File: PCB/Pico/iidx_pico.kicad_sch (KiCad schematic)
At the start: 77 parts, among them J1 Spin, J2 Spin, J3 RGB, J4 RGB, J5 Spin, J6 Spin, SW1 SWITCH_SPST, SW10 SWITCH_SPST, SW11 SWITCH_SPST, SW12 Tact_4pin, SW13 Tact_4pin, SW2 SWITCH_SPST, SW3 SWITCH_SPST, SW4 SWITCH_SPST, SW5 SWITCH_SPST, SW6 SWITCH_SPST, SW7 SWITCH_SPST, SW8 SWITCH_SPST, SW9 SWITCH_SPST, U1 PiPico_No_SWD, U2 TMAG5273, U3 AS5600

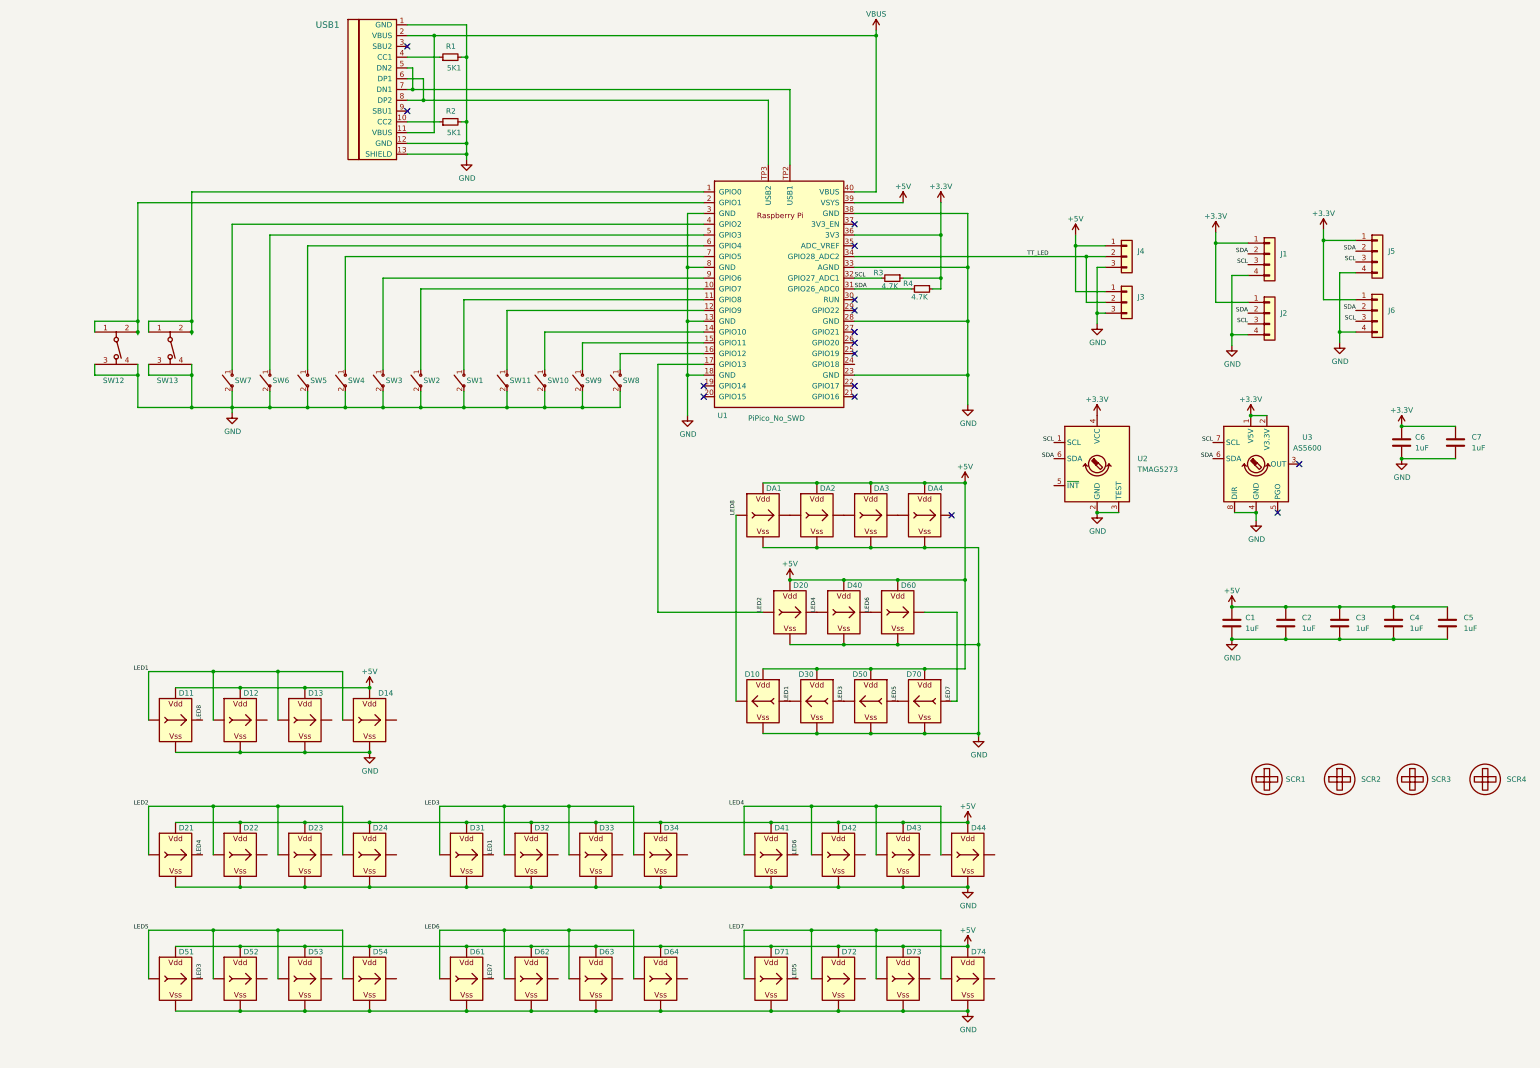
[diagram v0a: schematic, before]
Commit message: Hall effect switch support
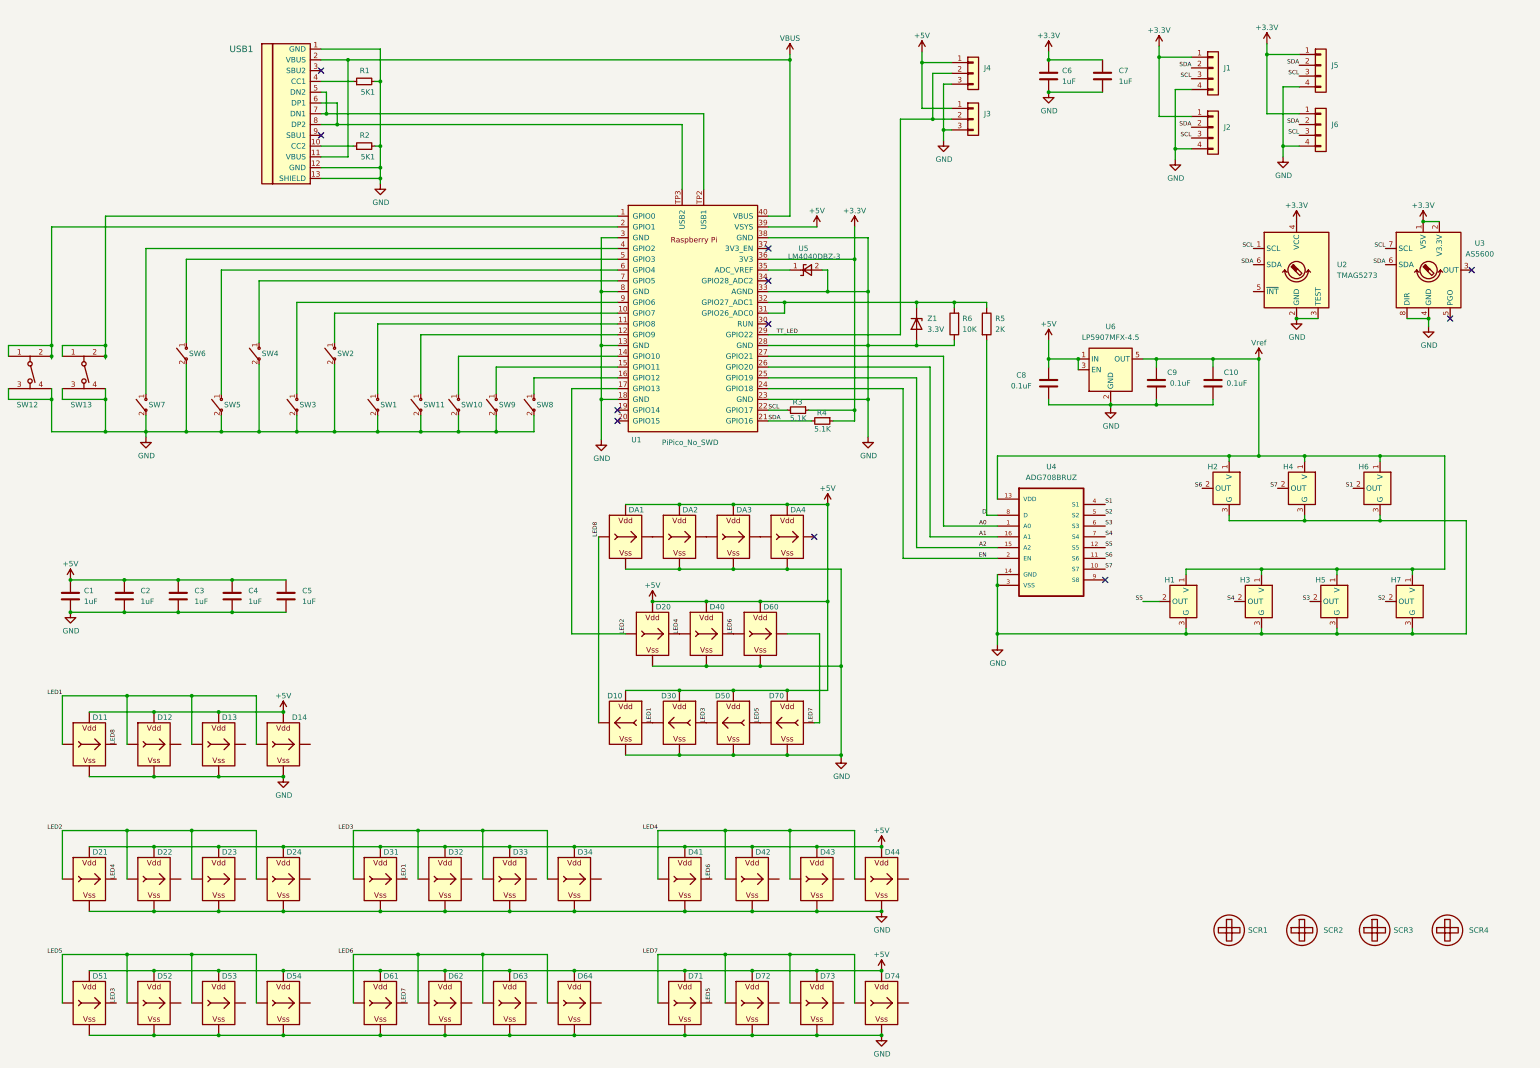
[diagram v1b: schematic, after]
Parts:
- added C10, C8, C9: 0.1uF, Capacitor_SMD:C_0603_1608Metric_Pad1.08x0.95mm_HandSolder, symbol Device:C
- added H1, H2, H3, H4, H5, H6, H7: SS49E_SOT23, iidx_pico:SOT-23-FAT, symbol iidx_pico:SS49E_SOT23
- added R5: 2K, Resistor_SMD:R_0603_1608Metric_Pad0.98x0.95mm_HandSolder, symbol Device:R
- added R6: 10K, Resistor_SMD:R_0603_1608Metric_Pad0.98x0.95mm_HandSolder, symbol Device:R
- added U4: ADG708BRUZ, Package_SO:TSSOP-16_4.4x5mm_P0.65mm, symbol voltex_pico:ADG708BRUZ
- added U5: LM4040DBZ-3, iidx_pico:SOT-23-FAT, symbol Reference_Voltage:LM4040DBZ-3
- added U6: LP5907MFX-4.5, Package_TO_SOT_SMD:SOT-23-5, symbol Regulator_Linear:LP5907MFX-4.5
- added Z1: 3.3V, Diode_SMD:D_SOD-123F, symbol Device:D_Zener
- R3, R4: value 4.7K -> 5.1K
- SW1, SW2, SW3, SW4, SW5, SW6, SW7: footprint iidx_pico:SW_Kailh_Choc_V1V2_IIDX -> iidx_pico:SW_Kailh_Choc_HE_IIDX
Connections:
- net +5V: now also C8.1, U6.1 (IN), U6.3 (EN)
- net GND: now also C10.2, C8.2, C9.2, H1.3 (G), H2.3 (G), H3.3 (G), H4.3 (G), H5.3 (G), H6.3 (G), H7.3 (G), R6.1, U4.14 (GND), U4.3 (VSS), U5.2 (A), U6.2 (GND), Z1.2 (A)
- net SCL: now also U1.22 (GPIO17); no longer U1.32 (GPIO27_ADC1)
- net SDA: now also U1.21 (GPIO16); no longer U1.31 (GPIO26_ADC0)
- net TT_LED: now also U1.29 (GPIO22); no longer U1.34 (GPIO28_ADC2)
- net EN: now reaches U1.24 (GPIO18)
- net EN: now also U4.2 (EN)
- net A2: now reaches U1.25 (GPIO19)
- net A2: now also U4.15 (A2)
- net A1: now reaches U1.26 (GPIO20)
- net A1: now also U4.16 (A1)
- net A0: now reaches U1.27 (GPIO21)
- net A0: now also U4.1 (A0)
- net at U1.35 (ADC_VREF): now also U5.1 (K)
- new net: R5.1, R6.2, U1.31 (GPIO26_ADC0), U1.32 (GPIO27_ADC1), Z1.1 (K)
- new net D: R5.2, U4.8 (D)
- new net S1: H6.2 (OUT), U4.4 (S1)
- new net S2: H7.2 (OUT), U4.5 (S2)
- new net S3: H5.2 (OUT), U4.6 (S3)
- new net S4: H3.2 (OUT), U4.7 (S4)
- new net S5: H1.2 (OUT), U4.12 (S5)
- new net S6: H2.2 (OUT), U4.11 (S6)
- new net S7: H4.2 (OUT), U4.10 (S7)
- new net Vref: C10.1, C9.1, H1.1 (V), H2.1 (V), H3.1 (V), H4.1 (V), H5.1 (V), H6.1 (V), H7.1 (V), U4.13 (VDD), U6.5 (OUT)
- no-connect marks 16 -> 11
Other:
- moved on the sheet: C1, C2, C3, C4, C5, C6, C7, D10, D11, D12, D13, D14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

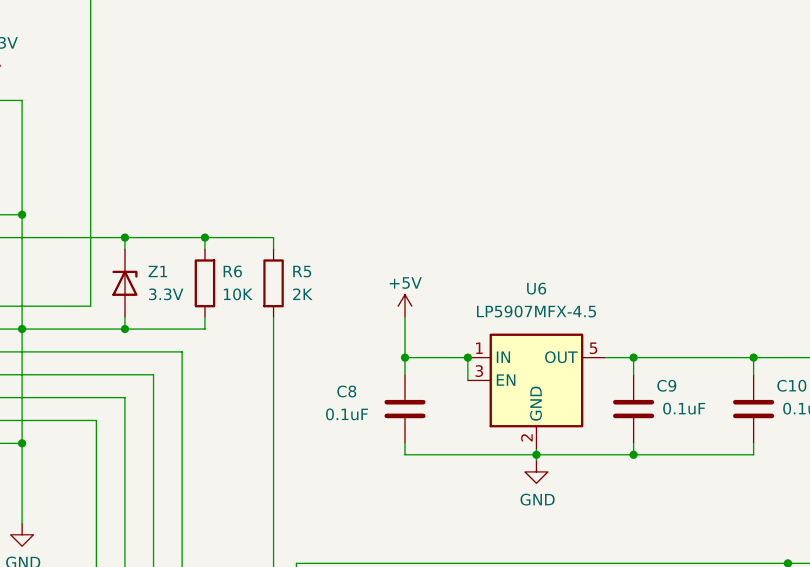
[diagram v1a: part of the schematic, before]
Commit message: PCB Pico v1.53 (vref from vbus)
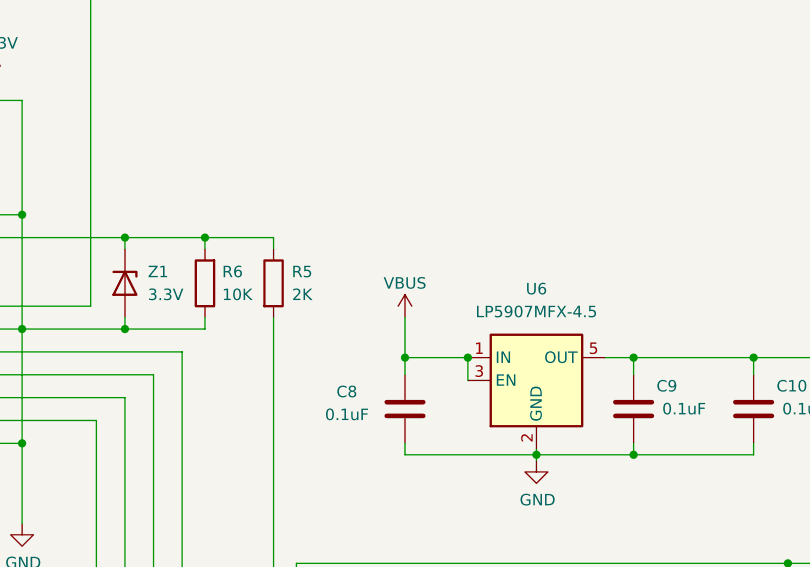
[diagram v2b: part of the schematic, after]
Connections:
- net +5V: no longer C8.1, U6.1 (IN), U6.3 (EN)
- net VBUS: now also C8.1, U6.1 (IN), U6.3 (EN)
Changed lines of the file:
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@@
-	)
-	(symbol
-		(lib_id "power:+5V")
-		(at 277.495 100.965 0)
-		(unit 1)
-		(exclude_from_sim no)
-		(in_bom yes)
-		(on_board yes)
-		(dnp no)
-		(property "Reference" "#PWR016"
-			(at 277.495 104.775 0)
-			(effects
-				(font
-					(size 1.27 1.27)
-				)
-				(hide yes)
-			)
-		)
-		(property "Value" "+5V"
-			(at 277.495 97.155 0)
-			(effects
-				(font
-					(size 1.27 1.27)
-				)
-			)
-		)
-		(property "Footprint" ""
-			(at 277.495 100.965 0)
-			(effects
-				(font
-					(size 1.27 1.27)
-				)
-				(hide yes)
-			)
-		)
-		(property "Datasheet" ""
-			(at 277.495 100.965 0)
-			(effects
-				(font
-					(size 1.27 1.27)
-				)
-				(hide yes)
-			)
-		)
-		(property "Description" ""
-			(at 277.495 100.965 0)
-			(effects
-				(font
-					(size 1.27 1.27)
-				)
-				(hide yes)
-			)
-		)
-		(pin "1"
-		)
-		(instances
-			(project "iidx_pico"
-				(path "/2e3f5573-c264-4a8b-a2f0-0e6473d39aad"
-					(reference "#PWR016")
-					(unit 1)
-				)
-			)
-		)
 	)
 	(symbol
@@
 					(unit 1)
 				)
+			)
+		)
+	)
+	(symbol
+		(lib_id "power:+5V")
+		(at 277.495 100.965 0)
+		(unit 1)
+		(exclude_from_sim no)
+		(in_bom yes)
+		(on_board yes)
+		(dnp no)
+		(property "Reference" "#PWR016"
+			(at 277.495 104.775 0)
+			(effects
+				(font
+					(size 1.27 1.27)
+				)
+				(hide yes)
+			)
+		)
+		(property "Value" "VBUS"
+			(at 277.495 97.155 0)
+			(effects
+				(font
+					(size 1.27 1.27)
+				)
+			)
+		)
+		(property "Footprint" ""
+			(at 277.495 100.965 0)
+			(effects
+				(font
+					(size 1.27 1.27)
+				)
+				(hide yes)
+			)
+		)
+		(property "Datasheet" ""
+			(at 277.495 100.965 0)
+			(effects
+				(font
+					(size 1.27 1.27)
+				)
+				(hide yes)
+			)
+		)
+		(property "Description" ""
+			(at 277.495 100.965 0)
+			(effects
+				(font
+					(size 1.27 1.27)
+				)
+				(hide yes)
+			)
+		)
+		(pin "1"
+		)
+		(instances
+			(project "iidx_pico"
+				(path "/2e3f5573-c264-4a8b-a2f0-0e6473d39aad"
+					(reference "#PWR016")
+					(unit 1)
+				)

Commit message: Update PCB v1.6 files missed
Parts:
- added JP1: DIR, Jumper:SolderJumper-2_P1.3mm_Open_RoundedPad1.0x1.5mm, symbol Jumper:SolderJumper_2_Open
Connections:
- net GND: now also JP1.2 (B); no longer U3.8 (DIR)
- new net: JP1.1 (A), U3.8 (DIR)
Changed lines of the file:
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@@
 	)
 	(junction
+		(at 369.57 99.695)
+		(diameter 0)
+		(color 0 0 0 0)
+	)
+	(junction
 		(at 203.2 183.515)
 		(diameter 0)
@@
 	)
 	(junction
-		(at 367.03 95.885)
-		(diameter 0)
-		(color 0 0 0 0)
-	)
-	(junction
 		(at 309.88 170.18)
 		(diameter 0)
@@
 	(wire
 		(pts
+			(xy 369.57 99.695) (xy 369.57 101.6)
+		)
+		(stroke
+			(width 0)
+			(type default)
+		)
+	)
+	(wire
+		(pts
 			(xy 332.74 57.785) (xy 332.74 55.245)
 		)
@@
 	(wire
 		(pts
-			(xy 367.03 97.79) (xy 367.03 95.885)
-		)
-		(stroke
-			(width 0)
-			(type default)
-		)
-	)
-	(wire
-		(pts
 			(xy 207.645 264.795) (xy 222.885 264.795)
 		)
@@
 	(wire
 		(pts
+			(xy 361.95 95.885) (xy 361.95 99.695)
+		)
+		(stroke
+			(width 0)
+			(type default)
+		)
+	)
+	(wire
+		(pts
 			(xy 42.545 104.775) (xy 42.545 105.41)
 		)
@@
 	(wire
 		(pts
+			(xy 369.57 95.885) (xy 367.03 95.885)
+		)
+		(stroke
+			(width 0)
+			(type default)
+		)
+	)
+	(wire
+		(pts
 			(xy 207.645 249.555) (xy 222.885 249.555)
 		)
@@
 	(wire
 		(pts
-			(xy 361.95 95.885) (xy 367.03 95.885)
-		)
-		(stroke
-			(width 0)
-			(type default)
-		)
-	)
-	(wire
-		(pts
 			(xy 277.495 107.315) (xy 277.495 105.41)
 		)
@@
 	(wire
 		(pts
+			(xy 369.57 95.885) (xy 369.57 99.695)
+		)
+		(stroke
+			(width 0)
+			(type default)
+		)
+	)
+	(wire
+		(pts
 			(xy 129.54 99.695) (xy 129.54 113.665)
 		)
@@
 	(symbol
 		(lib_id "power:GND")
-		(at 367.03 97.79 0)
+		(at 369.57 101.6 0)
 		(unit 1)
 		(exclude_from_sim no)
@@
 		(dnp no)
 		(property "Reference" "#PWR014"
-			(at 367.03 104.14 0)
+			(at 369.57 107.95 0)
 			(effects
 				(font
@@
 		)
 		(property "Value" "GND"
-			(at 367.157 102.1842 0)
+			(at 369.697 105.9942 0)
 			(effects
 				(font
@@
 		)
 		(property "Footprint" ""
-			(at 367.03 97.79 0)
+			(at 369.57 101.6 0)
 			(effects
 				(font
@@
 		)
 		(property "Datasheet" ""
-			(at 367.03 97.79 0)
+			(at 369.57 101.6 0)
 			(effects
 				(font
@@
 		)
 		(property "Description" ""
-			(at 367.03 97.79 0)
+			(at 369.57 101.6 0)
 			(effects
 				(font
@@
 					(unit 1)
 				)
+			)
+		)
+	)
+	(symbol
+		(lib_id "Jumper:SolderJumper_2_Open")
+		(at 365.76 99.695 0)
+		(unit 1)
+		(exclude_from_sim no)
+		(in_bom no)
+		(on_board yes)
+		(dnp no)
+		(property "Reference" "JP1"
+			(at 365.76 102.235 0)
+			(effects
+				(font
+					(size 1.27 1.27)
+				)
+			)
+		)
+		(property "Value" "DIR"
+			(at 365.76 95.885 0)
+			(effects
+				(font
+					(size 1.27 1.27)
+				)
+				(hide yes)
+			)
+		)
+		(property "Footprint" "Jumper:SolderJumper-2_P1.3mm_Open_RoundedPad1.0x1.5mm"
+			(at 365.76 99.695 0)
+			(effects
+				(font
+					(size 1.27 1.27)
+				)
+				(hide yes)
+			)
+		)
+		(property "Datasheet" "~"
+			(at 365.76 99.695 0)
+			(effects
+				(font
+					(size 1.27 1.27)
+				)
+				(hide yes)
+			)
+		)
+		(property "Description" "Solder Jumper, 2-pole, open"
+			(at 365.76 99.695 0)
+			(effects
+				(font
+					(size 1.27 1.27)
+				)
+				(hide yes)
+			)
+		)
+		(pin "2"
+		)
+		(pin "1"
+		)
+		(instances
+			(project ""
+				(path "/2e3f5573-c264-4a8b-a2f0-0e6473d39aad"
+					(reference "JP1")
+					(unit 1)
+				)
